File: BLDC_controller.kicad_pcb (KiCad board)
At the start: 4 copper layers, 50 x 38 mm, 371 parts, among them P2 CONN_01X06, P3 CONN_01X05, P5 CONN_01X05, Q1 PSMN2R0-30YLD, Q2 PSMN2R0-30YLD, Q3 PSMN2R0-30YLD, Q4 PSMN2R0-30YLD, Q5 PSMN2R0-30YLD, Q6 PSMN2R0-30YLD

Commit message: minor improvements
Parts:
- removed the REF** at (183.8, 86.7)
- removed the REF** at (166.6, 80.6)
- removed the REF** at (168.7, 79.9)
- removed the REF** at (167.9, 79.9)
- removed the REF** at (167.2, 79.9)
- removed the REF** at (166.6, 79.9)
- removed the REF** at (169.3, 79.2)
- removed the REF** at (167.2, 79.2)
- removed the REF** at (166.6, 79.2)
- removed the REF** at (167.6, 110.9)
- removed the REF** at (166.8, 110.9)
- removed the REF** at (173.0, 82.0)
- removed the REF** at (172.2, 91.2)
- removed the REF** at (170.9, 101.0)
- removed the REF** at (182.0, 81.3)
- removed the REF** at (138.5, 81.2)
- removed the REF** at (182.0, 112.8)
- removed the REF** at (138.5, 112.8)
- removed the REF** at (183.8, 103.9)
- added R48: 560R, project_footprints:R_0603, F.Cu at (139.0, 97.0)
- added REF**: VIA-0.8mm-0.4mm, project_footprints:VIA-0.8mm-0.4mm, F.Cu at (176.3, 84.6)
- added REF**: VIA-0.8mm-0.4mm, project_footprints:VIA-0.8mm-0.4mm, F.Cu at (169.9, 101.0)
- added REF**: PH_1.5mm, project_footprints:PH_1.5mm, F.Cu at (183.8, 85.5)
- added REF**: PH_0.8mm, project_footprints:PH_0.8mm, F.Cu at (172.5, 79.2)
- added REF**: PH_1.5mm, project_footprints:PH_1.5mm, F.Cu at (165.5, 79.5)
- added REF**: MountingHole_2.7mm, project_footprints:MountingHole_2.7mm, F.Cu at (138.2, 113.0)
- added REF**: MountingHole_2.7mm, project_footprints:MountingHole_2.7mm, F.Cu at (182.2, 113.0)
- added REF**: MountingHole_2.7mm, project_footprints:MountingHole_2.7mm, F.Cu at (182.2, 81.0)
- added REF**: MountingHole_2.7mm, project_footprints:MountingHole_2.7mm, F.Cu at (138.2, 81.0)
- added REF**: VIA-0.8mm-0.4mm, project_footprints:VIA-0.8mm-0.4mm, F.Cu at (173.8, 91.0)
- added REF**: PH_0.8mm, project_footprints:PH_0.8mm, F.Cu at (167.5, 79.2)
- added REF**: PH_1.5mm, project_footprints:PH_1.5mm, F.Cu at (173.2, 81.0)
- added REF**: PH_1.5mm, project_footprints:PH_1.5mm, F.Cu at (183.8, 102.8)
- added REF**: PH_1.5mm, project_footprints:PH_1.5mm, F.Cu at (183.8, 94.2)
- added V8: LED_ALT, project_footprints:LED_0402, F.Cu at (139.0, 99.8)
- moved C14 1.12 mm to (151.6, 102.0)
- moved C13 1.03 mm to (153.5, 91.8)
- moved R12 1.03 mm to (163.8, 94.3)
- moved C1 1.00 mm to (160.6, 85.7)
- moved C10 1.00 mm to (161.0, 96.8)
- moved C11 1.00 mm to (160.5, 86.4)
- moved C12 1.00 mm to (147.6, 99.9)
- moved C15 1.00 mm to (145.6, 94.5)
- moved C16 1.00 mm to (149.3, 91.3)
- moved C17 1.00 mm to (148.3, 102.1)
- moved C2 1.00 mm to (163.7, 96.9)
- moved C21 1.00 mm to (145.6, 96.8)
- moved C22 1.00 mm to (143.6, 87.9)
- moved C23 1.00 mm to (147.6, 87.9)
- moved C24 1.00 mm to (151.6, 87.9)
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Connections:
- D1 pad 13: (no net) -> /PA2
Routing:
- net +12V: track 62.5 -> 87.9 mm, vias 11 -> 9
- net /PA2: track 0.00 -> 19.6 mm, vias 0 -> 2
- net V_SENSE_P: track 15.2 -> 24.2 mm
- net U_SENSE_P: track 19.8 -> 27.4 mm
- net +3V3: track 28.0 -> 35.2 mm, vias 9 -> 11
- net /OUTU: track 51.5 -> 57.7 mm, vias 2 -> 1
- net /OUTV: track 35.0 -> 40.4 mm, vias 2 -> 1
- net /OUTW: track 37.4 -> 42.7 mm, vias 2 -> 1
- net /V_ADC: track 22.4 -> 18.7 mm
- net W_SENSE_P: track 19.1 -> 22.6 mm
- net /LSV: track 20.6 -> 23.4 mm
- net /LSU: track 20.4 -> 22.6 mm
- net GND: track 124.4 -> 122.5 mm, vias 28 -> 26
- net /PA2_LED: track 0.00 -> 1.59 mm
- net /OP2N: track 12.0 -> 13.4 mm
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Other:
- rule solder_mask_min_width: 0.1 -> 0.0999

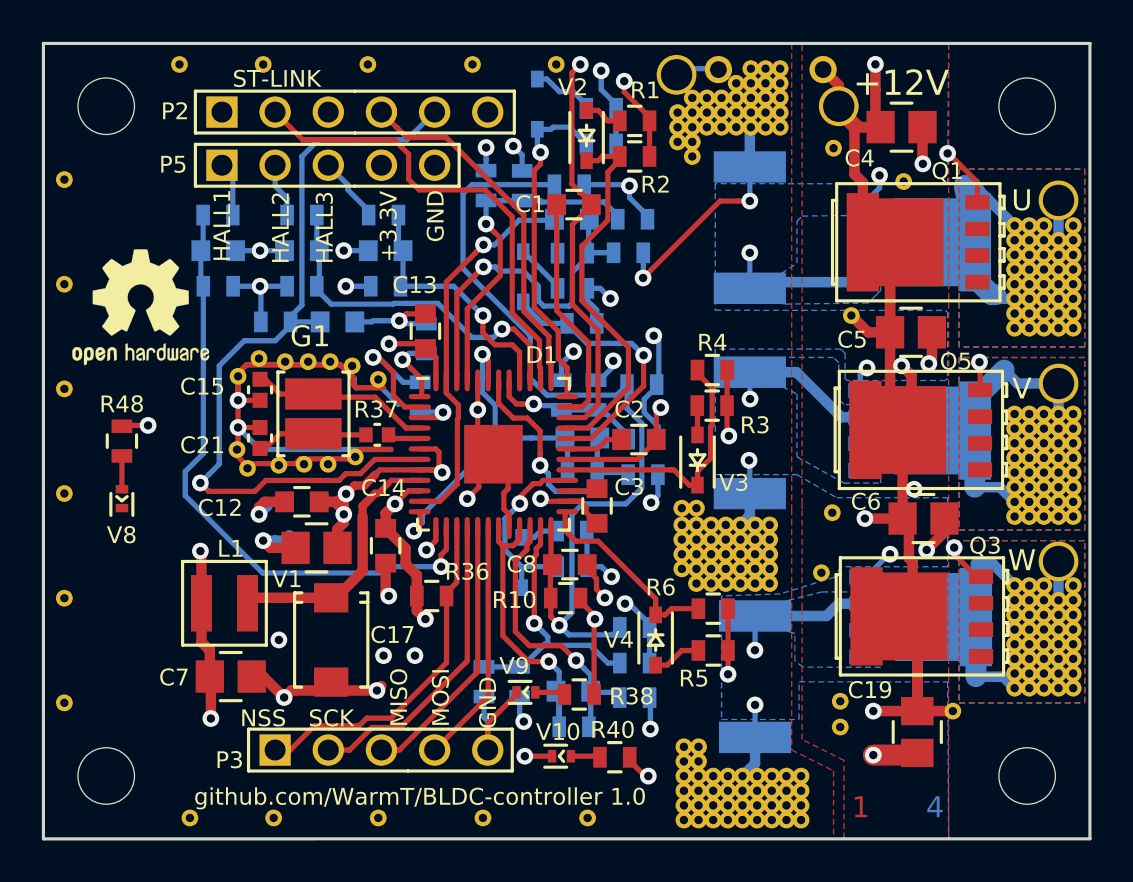
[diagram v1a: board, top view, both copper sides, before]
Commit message: self-intersecting polygons
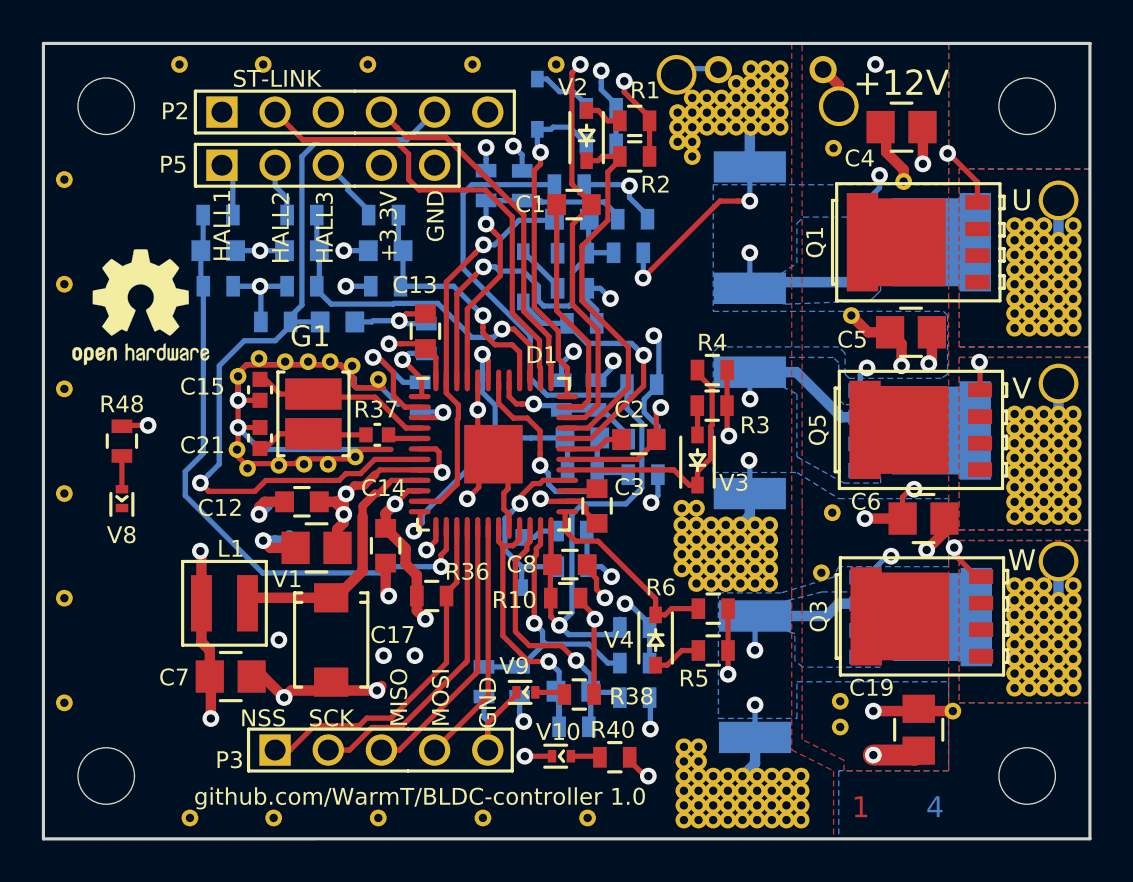
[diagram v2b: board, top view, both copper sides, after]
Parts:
- moved C19 0.13 mm to (177.1, 110.8)
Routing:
- net +12V: track 87.9 -> 32.3 mm, vias 9 -> 8
- net /OUTV: track 40.4 -> 29.1 mm
- net /OUTU: track 57.7 -> 47.4 mm
- net /OUTW: track 42.7 -> 32.9 mm
- net (no net): vias 3 -> 4
